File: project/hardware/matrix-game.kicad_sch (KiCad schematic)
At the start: 31 parts, among them SW1 button_center, SW2 button_left, SW3 button_down, SW4 button_right, SW5 button_up, U1 NUCLEO-F042K6, U2 MAX7219, U3 SSD1306

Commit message: [project/hardware/layout] more layouting
Signed-off-by: Timon Burkard <timon.burkard@gwf.ch>
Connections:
- net lcd_scl: now reaches U1.CN3_11 (PF1/D8), U3.3 (SCL)
- no-connect marks 0 -> 16
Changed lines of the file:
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@@
 		(color 0 0 0 0)
 	)
+	(no_connect
+		(at 149.86 76.2)
+	)
+	(no_connect
+		(at 149.86 104.14)
+	)
+	(no_connect
+		(at 109.22 91.44)
+	)
+	(no_connect
+		(at 149.86 81.28)
+	)
+	(no_connect
+		(at 149.86 91.44)
+	)
+	(no_connect
+		(at 109.22 93.98)
+	)
+	(no_connect
+		(at 109.22 111.76)
+	)
+	(no_connect
+		(at 109.22 99.06)
+	)
+	(no_connect
+		(at 199.39 76.2)
+	)
+	(no_connect
+		(at 109.22 78.74)
+	)
+	(no_connect
+		(at 109.22 76.2)
+	)
+	(no_connect
+		(at 149.86 106.68)
+	)
+	(no_connect
+		(at 149.86 111.76)
+	)
+	(no_connect
+		(at 149.86 86.36)
+	)
+	(no_connect
+		(at 109.22 81.28)
+	)
+	(no_connect
+		(at 149.86 101.6)
+	)
 	(wire
 		(pts
@@
 	(wire
 		(pts
-			(xy 109.22 101.6) (xy 99.06 101.6)
-		)
-		(stroke
-			(width 0)
-			(type default)
-		)
-	)
-	(wire
-		(pts
 			(xy 213.36 63.5) (xy 273.05 63.5)
 		)
@@
 	(wire
 		(pts
-			(xy 99.06 140.97) (xy 207.01 140.97)
-		)
-		(stroke
-			(width 0)
-			(type default)
-		)
-	)
-	(wire
-		(pts
 			(xy 193.04 101.6) (xy 193.04 105.41)
 		)
@@
 	(wire
 		(pts
-			(xy 99.06 101.6) (xy 99.06 140.97)
-		)
-		(stroke
-			(width 0)
-			(type default)
-		)
-	)
-	(wire
-		(pts
 			(xy 91.44 119.38) (xy 93.98 119.38)
 		)
@@
 	(wire
 		(pts
-			(xy 207.01 140.97) (xy 207.01 146.05)
-		)
-		(stroke
-			(width 0)
-			(type default)
-		)
-	)
-	(wire
-		(pts
 			(xy 220.98 68.58) (xy 220.98 74.93)
 		)
@@
 	(wire
 		(pts
+			(xy 207.01 142.24) (xy 207.01 146.05)
+		)
+		(stroke
+			(width 0)
+			(type default)
+		)
+	)
+	(wire
+		(pts
 			(xy 172.72 48.26) (xy 172.72 52.07)
 		)
@@
 	(wire
 		(pts
+			(xy 93.98 101.6) (xy 109.22 101.6)
+		)
+		(stroke
+			(width 0)
+			(type default)
+		)
+	)
+	(wire
+		(pts
 			(xy 199.39 38.1) (xy 205.74 38.1)
 		)
@@
 	(wire
 		(pts
+			(xy 187.96 142.24) (xy 207.01 142.24)
+		)
+		(stroke
+			(width 0)
+			(type default)
+		)
+	)
+	(wire
+		(pts
 			(xy 280.67 35.56) (xy 261.62 35.56)
 		)
@@
 		)
 	)
+	(global_label "lcd_scl"
+		(shape input)
+		(at 93.98 101.6 180)
+		(fields_autoplaced yes)
+		(effects
+			(font
+				(size 1.27 1.27)
+			)
+			(justify right)
+		)
+		(property "Intersheetrefs" "${INTERSHEET_REFS}"
+			(at 84.3425 101.6 0)
+			(effects
+				(font
+					(size 1.27 1.27)
+				)
+				(justify right)
+				(hide yes)
+			)
+		)
+	)
+	(global_label "lcd_scl"
+		(shape input)
+		(at 187.96 142.24 180)
+		(fields_autoplaced yes)
+		(effects
+			(font
+				(size 1.27 1.27)
+			)
+			(justify right)
+		)
+		(property "Intersheetrefs" "${INTERSHEET_REFS}"
+			(at 178.3225 142.24 0)
+			(effects
+				(font
+					(size 1.27 1.27)
+				)
+				(justify right)
+				(hide yes)
+			)
+		)
+	)

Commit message: [project/hardware/schematic] added labels
Signed-off-by: Timon Burkard <timon.burkard@gwf.ch>
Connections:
- net lcd_sda: now reaches U1.CN3_5 (PA12/D2), U3.4 (SDA)
- net max_mosi: now reaches U1.CN3_14 (PB5/D11), U2.1 (DIN)
- net max_cs: now reaches U1.CN3_13 (PA11/D10), U2.12 (LOAD)
- net max_clk: now reaches U1.CN4_8 (PA5/A4), U2.13 (CLK)
- net button_left: now reaches SW2.2, U1.CN3_9 (PB1/D6)
- net button_right: now reaches SW4.2, U1.CN3_12 (PA8/D9)
- net button_center: now reaches SW1.2, U1.CN3_6 (PB0/D3)
- net button_down: now reaches SW3.2, U1.CN4_10 (PA3/A2)
- net button_up: now reaches SW5.2, U1.CN4_6 (PA7/A6)
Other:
- moved on the sheet: BZ1, C1, C2, D1, JP1, R1, SW1, SW2, SW3, SW4, SW5, TP1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

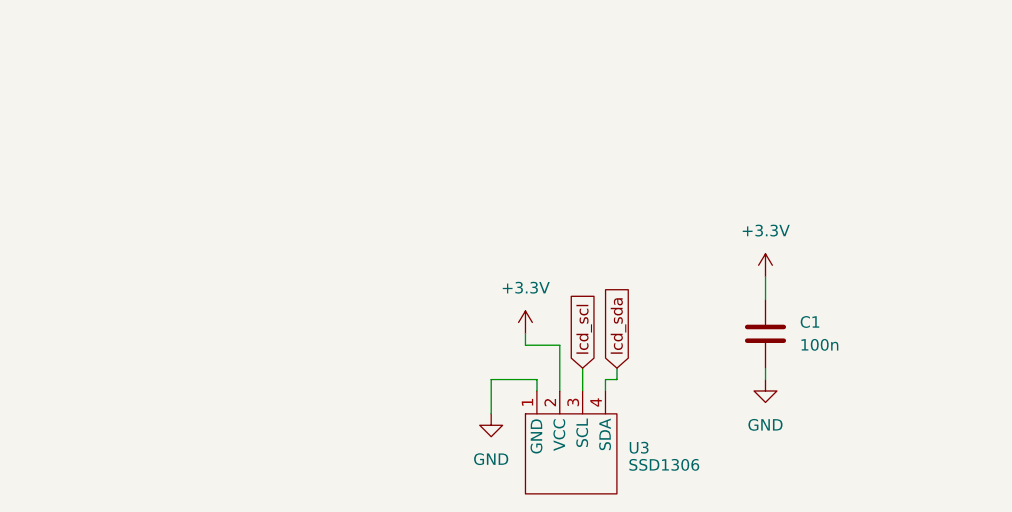
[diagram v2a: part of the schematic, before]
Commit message: [project/hardware] added library model for LCD, added sockets for Nucleo and LCD
Signed-off-by: Timon Burkard <timon.burkard@gwf.ch>
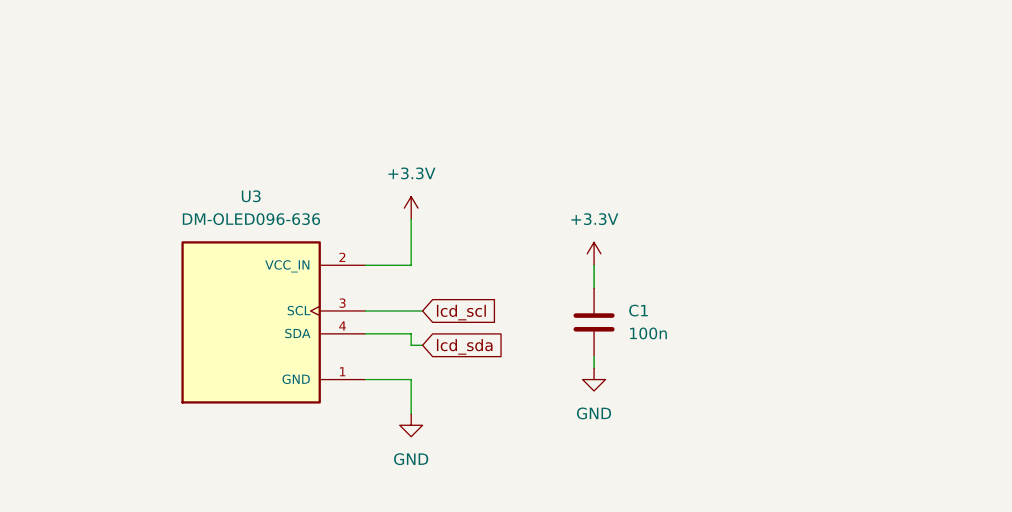
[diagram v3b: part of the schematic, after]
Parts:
- removed U3: SSD1306, Custom_Library:LCD_I2C, symbol Custom_Library:LCD_I2C
- added U3: DM-OLED096-636, DM-OLED096-636:MODULE_DM-OLED096-636, symbol lcd:DM-OLED096-636
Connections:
- net +3.3V: now also U3.2 (VCC_IN)
- net GND: now also U3.1 (GND)
- net lcd_scl: now also U3.3 (SCL)
- net lcd_sda: now also U3.4 (SDA)
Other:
- moved on the sheet: C1
